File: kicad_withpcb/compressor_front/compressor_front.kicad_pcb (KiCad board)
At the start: 2 copper layers, 35 x 110 mm, 33 parts, among them J1 MAIN BOARD, SW1 BYPASS, SW2 INT/EXT, SW3 HPF DEFEAT, SW4 LINK, U10 LM3915, U9 LM3914

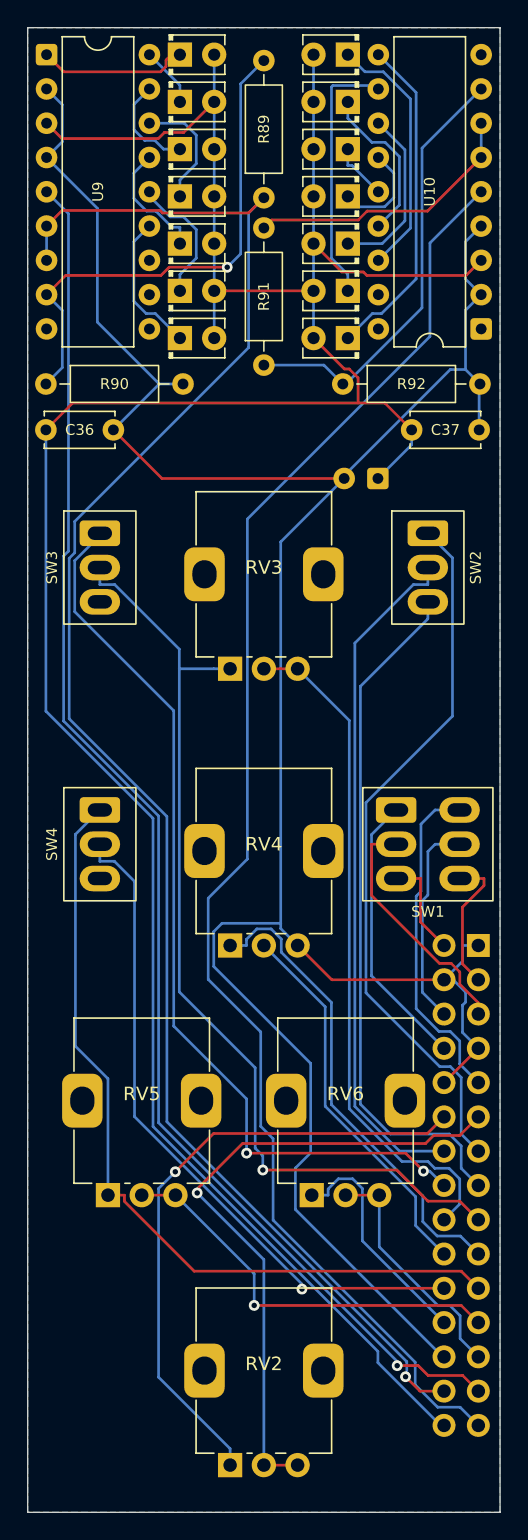
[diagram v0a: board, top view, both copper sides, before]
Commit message: Simulate the compressor, fix its values, and fit Altronics parts (#5)
* Make the schematic simulate in KiCad, and add the simulation results

Every part on the kicad/ sheets now has a SPICE model (Sim.* fields, models in
kicad/sim/compressor_models.lib), the connectors are excluded from simulation, and the
root sheet carries a test bench: the rack's supplies, a balanced source, a load and the
knob settings as .param lines. The netlist is unchanged.

tools/add_sim_models.py writes the fields. tools/sim/run_all.py exports the netlist with
kicad-cli and runs the characterisation in ngspice; kicad/sim/README.md has how to run
it in KiCad and what it found.

* Bring the compressor's values in line with the design targets

Through gain: R21/R22 3k3 to 6k8 halves the recovery amp's gain, so the
module is unity balanced in to out and BYPASS matches; R36 100k to 200k
keeps the detector's level. Bass: C9/C10 2u2 to 4u7 with the larger
input resistors puts the -3 dB point near 5 Hz.
Threshold: RV3 1M linear to 250k audio taper and R35 20k to 2k4 spread
about -20 to +20 dBu over the knob. R60 47k to 24k sets the resting
steer near 150 mV.
Timing: R45/R46/RV5 and R47/RV6/R74 scaled up to match the RC targets
with the same C15.

Same changes on the sheets, both boards and design.py. The simulation's
pot model gains an audio taper, and the burst test now runs at half
threshold.

* Carry the new values onto both boards' schematics and layouts

* Retune attack and release: R45 220R, R46 47R, RV5 10k, R47 15k

The first pass ran the attack too slow (9 to 103 ms against a 2.7 to
50 ms target). Results are regenerated in the next commit.

* Regenerate the simulation results for the new values

* Stop the fast-attack overshoot: C22 47u to 4u7

C22 made STA lag STB by about 60 ms, so when CTRL-B pulled the
reference node down the steering kept moving after the control
voltage had settled, overshooting by up to 20 dB. With 4u7 the two
sides track and the overshoot is about 1 dB. RV5 back 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
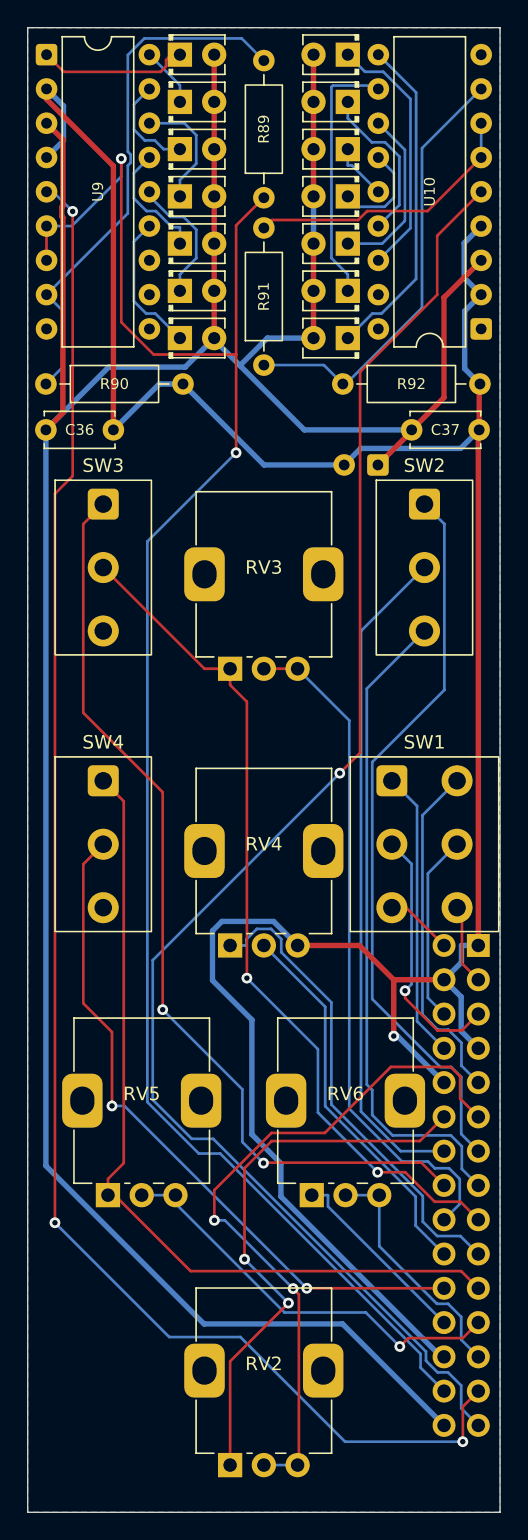
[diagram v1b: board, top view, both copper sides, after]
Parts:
- RV3: value 1M -> 100kA
- RV5: value 4k7 -> 10k
- RV6: value 220k -> 1M
- SW1: footprint compressor_front:SW_Toggle_SubMini_DPDT_Jaycar_ST0310 -> compressor_front:SW_Toggle_Mini_DPDT_Salecom_S1350
- SW2, SW3, SW4: footprint compressor_front:SW_Toggle_SubMini_SPDT_Jaycar_ST0300 -> compressor_front:SW_Toggle_Mini_SPDT_Salecom_S1315
- moved C38 1.00 mm to (127.5, 84.4)
- moved SW1 0.25 mm to (130.9, 112.5)
- moved SW2 0.25 mm to (130.9, 92.0)
- moved SW3 0.25 mm to (107.2, 92.0)
- moved SW4 0.25 mm to (107.2, 112.5)
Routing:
- net GR_METER: track 104.8 -> 119.2 mm, vias 1 -> 3
- net +16V: track 203.1 -> 215.2 mm
- net AGND: track 189.2 -> 198.7 mm, vias 0 -> 1
- net HPF_B: track 71.5 -> 63.3 mm, vias 1 -> 2
- net GR_REF: track 126.7 -> 134.6 mm, vias 1 -> 2
- net MAKEUP_FB: track 46.0 -> 41.5 mm, vias 1 -> 2
- net IN-: track 10.5 -> 5.99 mm
- net LVL_METER: track 109.0 -> 112.9 mm, vias 0 -> 1
- net OUT-A: track 48.0 -> 51.8 mm, vias 1 -> 2
- net TIMING: track 17.3 -> 14.2 mm
- net KEY: track 51.5 -> 48.8 mm
- net IN+: track 7.49 -> 5.02 mm
- net OUT-: track 15.4 -> 14.0 mm
- net HPF_A: track 67.6 -> 69.1 mm
- net LINK_SW: track 60.9 -> 62.3 mm
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
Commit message: Two LM3914 meters with ten LEDs each, simulated (#6)
* Swap the level meter's LM3915 for an LM3914 on outputs 1-7

Nobody stocks the LM3915, so U10 becomes a second LM3914. The LEDs move
to outputs 1-7 and outputs 8-10 join the top LED, giving a 17 dB scale
with no added parts. Front board LVL tracks re-routed; BOM regenerated.

* Give both meters ten LEDs and simulate them

Adds D27-D29 (GR outputs 8-10) and D37-D39 (LVL outputs 8-10) on all three
schematics. The front board's meter columns move to a 3.0 mm pitch with
LVL output 10 at the top; R90/R92 move to a 7.62 mm footprint and C38
turns to clear the LEDs; the affected nets were re-routed. R92 becomes 4k7
so RV8 can set the top LED at +18 dBu. The panel gets the six extra holes.
The LM3914 sim model now has its comparators and LED current sinks, and
tools/sim/meters.py simulates both meters.

* Write up the meter simulation
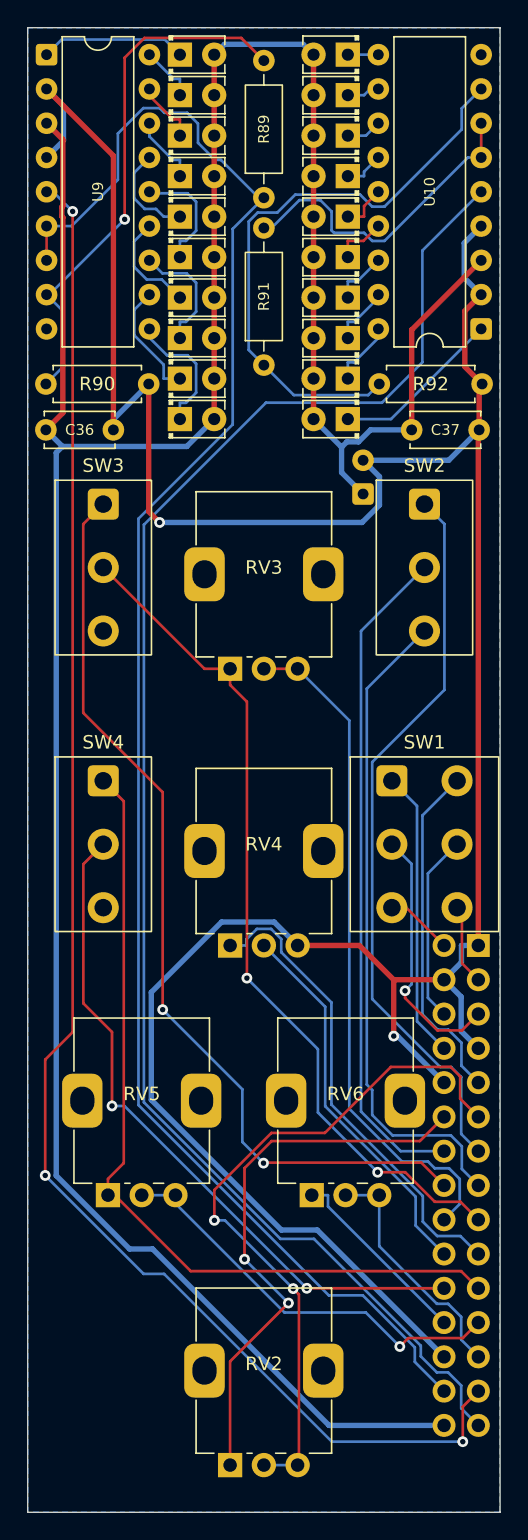
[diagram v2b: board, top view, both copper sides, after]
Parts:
- added D27: meter, LED_THT:LED_D2.0mm_W4.0mm_H2.8mm_FlatTop, F.Cu at (112.8, 75.0)
- added D28: meter, LED_THT:LED_D2.0mm_W4.0mm_H2.8mm_FlatTop, F.Cu at (112.8, 78.0)
- added D29: meter, LED_THT:LED_D2.0mm_W4.0mm_H2.8mm_FlatTop, F.Cu at (112.8, 81.0)
- added D37: meter, LED_THT:LED_D2.0mm_W4.0mm_H2.8mm_FlatTop, F.Cu at (125.3, 60.0)
- added D38: meter, LED_THT:LED_D2.0mm_W4.0mm_H2.8mm_FlatTop, F.Cu at (125.3, 57.0)
- added D39: meter, LED_THT:LED_D2.0mm_W4.0mm_H2.8mm_FlatTop, F.Cu at (125.3, 54.0)
- R90: footprint Resistor_THT:R_Axial_DIN0207_L6.3mm_D2.5mm_P10.16mm_Horizontal -> Resistor_THT:R_Axial_DIN0207_L6.3mm_D2.5mm_P7.62mm_Horizontal
- R92: value 8k2 -> 4k7; footprint Resistor_THT:R_Axial_DIN0207_L6.3mm_D2.5mm_P10.16mm_Horizontal -> Resistor_THT:R_Axial_DIN0207_L6.3mm_D2.5mm_P7.62mm_Horizontal
- U10: value LM3915 -> LM3914
- moved D30 27.0 mm to (125.3, 81.0)
- moved D31 20.5 mm to (125.3, 78.0)
- moved D32 14.0 mm to (125.3, 75.0)
- moved D36 12.0 mm to (125.3, 63.0)
- moved D33 7.50 mm to (125.3, 72.0)
- moved D35 5.50 mm to (125.3, 66.0)
- moved D26 3.00 mm to (112.8, 72.0)
- moved R92 2.70 mm to (127.6, 78.4)
- moved D25 2.50 mm to (112.8, 69.0)
- moved C38 2.42 mm to (126.4, 86.5), turned to 90 degrees
- moved D24 2.00 mm to (112.8, 66.0)
- moved D23 1.50 mm to (112.8, 63.0)
- moved D22 1.00 mm to (112.8, 60.0)
- moved D34 1.00 mm to (125.3, 69.0)
- moved D21 0.50 mm to (112.8, 57.0)
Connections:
- U10 pad 1: unconnected-(U10-LED1-Pad1) -> LVL1
- U10 pad 10: LVL7 -> LVL10
- U10 pad 11: LVL6 -> LVL9
- U10 pad 12: LVL5 -> LVL8
- U10 pad 13: LVL4 -> LVL7
- U10 pad 14: LVL3 -> LVL6
- U10 pad 15: LVL2 -> LVL5
- U10 pad 16: LVL1 -> LVL4
- U10 pad 17: unconnected-(U10-LED3-Pad17) -> LVL3
- U10 pad 18: unconnected-(U10-LED2-Pad18) -> LVL2
- U9 pad 10: unconnected-(U9-LED10-Pad10) -> GR10
- U9 pad 11: unconnected-(U9-LED9-Pad11) -> GR9
- U9 pad 12: unconnected-(U9-LED8-Pad12) -> GR8
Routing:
- net LVL7: track 24.7 -> 3.02 mm
- net AGND: track 198.7 -> 217.1 mm, vias 1 -> 2
- net LVL6: track 19.2 -> 3.48 mm
- net LVL_REFADJ: track 32.7 -> 43.9 mm
- net GR10: track 0.00 -> 9.77 mm
- net LVL5: track 13.0 -> 3.92 mm
- net GR8: track 0.00 -> 9.01 mm
- net GR9: track 0.00 -> 8.79 mm
- net LVL2: track 12.0 -> 4.88 mm
- net LVL1: track 18.9 -> 12.6 mm
- net LVL_METER: track 112.9 -> 119.0 mm, vias 1 -> 0
- net GR4: track 8.88 -> 5.16 mm
- net GR_REF: track 134.6 -> 130.9 mm, vias 2 -> 0
- net LVL4: track 7.46 -> 4.11 mm
- net LVL_REF: track 20.8 -> 24.1 mm
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
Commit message: Re-route the main board, reverse RATIO, and re-plot the Gerbers for both boards (#7)
* Re-plot the Gerbers for both boards from the current layout

The committed main-board Gerbers were plotted on 2026-10-01, before the film-cap
re-place and re-route, so 119 of their holes no longer match the board. Re-plot
them from the current board, add the front board's set, and zip each for the fab.

tools/plot_fab.sh does both boards in one go so the zips can be refreshed after
every board change. The README gets an Ordering section with the fab settings.

* Re-route the main board: paired IN/OUT, one-piece ground pour

IN+/IN- and OUT+/OUT- run as pairs 0.6 mm apart on the top layer, with
one via each on IN- and OUT- beside the edge fingers. Most other tracks
moved to the top so the bottom AGND pour is one piece (was seven).
DRC 0 errors, 0 unconnected, 0 schematic parity issues. Gerbers re-plotted.

* Swap RATIO's outer pins so clockwise gives a harder ratio

RV4 pin 1 is now AGND and pin 3 RATIO_CW on all three schematics and the
front board (symbol mirrored, front-board tracks re-routed at RV4).
The sim model reads POS={1-RATIO}, so RATIO keeps its meaning and the
results are unchanged. Front-board DRC 0 errors, 0 unconnected, 0 parity;
front Gerbers re-plotted.
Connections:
- RV4 pad 1: RATIO_CW -> AGND
- RV4 pad 3: AGND -> RATIO_CW
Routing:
- net RATIO_CW: track 35.3 -> 29.4 mm
- net AGND: track 217.1 -> 220.6 mm
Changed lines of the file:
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@@
 			(layers "*.Cu" "*.Mask")
 			(remove_unused_layers no)
-			(net "RATIO_CW")
+			(net "AGND")
 		)
 		(pad "2" thru_hole circle
@@
 			(layers "*.Cu" "*.Mask")
 			(remove_unused_layers no)
-			(net "AGND")
+			(net "RATIO_CW")
 		)
 		(pad "MP" thru_hole roundrect
@@
 	)
 	(gr_circle
-		(center 114.1 54) (end 115.2 54)
+		(center 114.1 54)
+		(end 115.2 54)
 		(stroke
 			(width 0.1)
@@
 	)
 	(gr_circle
-		(center 114.1 57) (end 115.2 57)
+		(center 114.1 57)
+		(end 115.2 57)
 		(stroke
 			(width 0.1)
@@
 	)
 	(gr_circle
-		(center 114.1 60) (end 115.2 60)
+		(center 114.1 60)
+		(end 115.2 60)
 		(stroke
 			(width 0.1)
@@
 	)
 	(gr_circle
-		(center 114.1 63) (end 115.2 63)
+		(center 114.1 63)
+		(end 115.2 63)
 		(stroke
 			(width 0.1)
@@
 	)
 	(gr_circle
-		(center 114.1 66) (end 115.2 66)
+		(center 114.1 66)
+		(end 115.2 66)
 		(stroke
 			(width 0.1)
@@
 	)
 	(gr_circle
-		(center 114.1 69) (end 115.2 69)
+		(center 114.1 69)
+		(end 115.2 69)
 		(stroke
 			(width 0.1)
@@
 	)
 	(gr_circle
-		(center 114.1 72) (end 115.2 72)
+		(center 114.1 72)
+		(end 115.2 72)
 		(stroke
 			(width 0.1)
@@
 	)
 	(gr_circle
-		(center 114.1 75) (end 115.2 75)
+		(center 114.1 75)
+		(end 115.2 75)
 		(stroke
 			(width 0.1)
@@
 	)
 	(gr_circle
-		(center 114.1 78) (end 115.2 78)
+		(center 114.1 78)
+		(end 115.2 78)
 		(stroke
 			(width 0.1)
@@
 	)
 	(gr_circle
-		(center 114.1 81) (end 115.2 81)
+		(center 114.1 81)
+		(end 115.2 81)
 		(stroke
 			(width 0.1)
@@
 	)
 	(gr_circle
-		(center 124 54) (end 125.1 54)
+		(center 119.05 43.96)
+		(end 120.64 43.96)
 		(stroke
 			(width 0.1)
@@
 	)
 	(gr_circle
-		(center 124 57) (end 125.1 57)
+		(center 119.05 43.96)
+		(end 121.91 43.96)
 		(stroke
 			(width 0.1)
@@
 	)
 	(gr_circle
-		(center 124 60) (end 125.1 60)
+		(center 119.05 92)
+		(end 122.65 92)
 		(stroke
 			(width 0.1)
@@
 	)
 	(gr_circle
-		(center 124 63) (end 125.1 63)
+		(center 119.05 112.5)
+		(end 122.65 112.5)
 		(stroke
 			(width 0.1)
@@
 	)
 	(gr_circle
-		(center 124 66) (end 125.1 66)
+		(center 119.05 151)
+		(end 122.65 151)
 		(stroke
 			(width 0.1)
@@
 	)
 	(gr_circle
-		(center 124 69) (end 125.1 69)
+		(center 119.05 169.39)
+		(end 120.64 169.39)
 		(stroke
 			(width 0.1)
@@
 	)
 	(gr_circle
-		(center 124 72) (end 125.1 72)
+		(center 119.05 169.39)
+		(end 121.91 169.39)
 		(stroke
 			(width 0.1)
@@
 	)
 	(gr_circle
-		(center 124 75) (end 125.1 75)
+		(center 124 54)
+		(end 125.1 54)
 		(stroke
 			(width 0.1)
@@
 	)
 	(gr_circle
-		(center 124 78) (end 125.1 78)
+		(center 124 57)
+		(end 125.1 57)
 		(stroke
 			(width 0.1)
@@
 	)
 	(gr_circle
-		(center 124 81) (end 125.1 81)
+		(center 124 60)
+		(end 125.1 60)
 		(stroke
 			(width 0.1)
@@
 	)
 	(gr_circle
-		(center 119.05 43.96)
-		(end 120.64 43.96)
+		(center 124 63)
+		(end 125.1 63)
 		(stroke
 			(width 0.1)
@@
 	)
 	(gr_circle
-		(center 119.05 43.96)
-		(end 121.91 43.96)
+		(center 124 66)
+		(end 125.1 66)
 		(stroke
 			(width 0.1)
@@
 	)
 	(gr_circle
-		(center 119.05 92)
-		(end 122.65 92)
+		(center 124 69)
+		(end 125.1 69)
 		(stroke
 			(width 0.1)
@@
 	)
 	(gr_circle
-		(center 119.05 112.5)
-		(end 122.65 112.5)
+		(center 124 72)
+		(end 125.1 72)
 		(stroke
 			(width 0.1)
@@
 	)
 	(gr_circle
-		(center 119.05 151)
-		(end 122.65 151)
+		(center 124 75)
+		(end 125.1 75)
 		(stroke
 			(width 0.1)
@@
 	)
 	(gr_circle
-		(center 119.05 169.39)
-		(end 120.64 169.39)
+		(center 124 78)
+		(end 125.1 78)
 		(stroke
 			(width 0.1)
@@
 	)
 	(gr_circle
-		(center 119.05 169.39)
-		(end 121.91 169.39)
+		(center 124 81)
+		(end 125.1 81)
 		(stroke
 			(width 0.1)
@@
 	)
 	(segment
-		(start 121.55 120)
-		(end 126.1318 120)
-		(width 0.4)
-		(layer "F.Cu")
-		(net "AGND")
-	)
-	(segment
 		(start 135.22 78.4)
 		(end 135 78.62)
@@
 	)
 	(segment
-		(start 126.1318 120)
-		(end 128.6718 122.54)
+		(start 135 78.62)
+		(end 135 81.8)
 		(width 0.4)
 		(layer "F.Cu")
@@
 	)
 	(segment
-		(start 135 78.62)
-		(end 135 81.8)
+		(start 128.6718 122.54)
+		(end 132.4 122.54)
 		(width 0.4)
 		(layer "F.Cu")
@@
 	)
 	(segment
-		(start 128.6718 122.54)
-		(end 132.4 122.54)
+		(start 116.55 120)
+		(end 116.55 123.6)
 		(width 0.4)
 		(layer "F.Cu")
@@
 	)
 	(segment
+		(start 116.55 123.6)
+		(end 127.6118 123.6)
+		(width 0.4)
+		(layer "F.Cu")
+		(net "AGND")
+	)
+	(segment
+		(start 127.6118 123.6)
+		(end 128.671799 122.54)
+		(width 0.4)
+		(layer "F.Cu")
+		(net "AGND")
+	)
+	(segment
 		(start 110.52 87.8563)
 		(end 111.3236 88.6599)
@@
 	)
 	(segment
+		(start 116.55 120)
+		(end 116.55 120)
+		(width 0.4)
+		(layer "B.Cu")
+		(net "AGND")
+	)
+	(segment
 		(start 135.15 66.7)
 		(end 133.8939 67.9561)
@@
 	)
 	(segment
+		(start 116.55 120)
+		(end 115.9162 118.265)
+		(width 0.4)
+		(layer "B.Cu")
+		(net "AGND")
+	)
+	(segment
 		(start 133.8939 67.9561)
 		(end 133.8939 70.5239)
@@
 	)
 	(segment
-		(start 119.815 118.265)
-		(end 121.55 120)
-		(width 0.4)
-		(layer "B.Cu")
-		(net "AGND")
-	)
-	(segment
 		(start 110.7097 131.4428)
 		(end 110.7097 123.4715)
@@
 	)
 	(segment
-		(start 115.9162 118.265)
-		(end 119.815 118.265)
-		(width 0.4)
-		(layer "B.Cu")
-		(net "AGND")
-	)
-	(segment
 		(start 132.4 122.54)
 		(end 133.6883 121.2517)
@@
 	)
 	(segment
-		(start 118.535 118.772)
-		(end 119.584 118.772)
-		(width 0.2)
-		(layer "B.Cu")
-		(net "RATIO_CW")
-	)
-	(segment
-		(start 117.762 120)
-		(end 117.762 119.546)
-		(width 0.2)
-		(layer "B.Cu")
-		(net "RATIO_CW")
-	)
-	(segment
 		(start 124.054 124.218)
 		(end 124.054 131.79)
@@
 	)
 	(segment
-		(start 117.762 119.546)
-		(end 118.535 118.772)
+		(start 121.55 121.714)
+		(end 124.054 124.218)
 		(width 0.2)
 		(layer "B.Cu")
@@
 	)
 	(segment
-		(start 120.338 119.526)
-		(end 120.338 120.502)
+		(start 121.55 120)
+		(end 121.55 121.714)
 		(width 0.2)
 		(layer "B.Cu")
@@
 	)
 	(segment
-		(start 119.584 118.772)
-		(end 120.338 119.526)
-		(width 0.2)
-		(layer "B.Cu")
-		(net "RATIO_CW")
-	)
-	(segment
-		(start 116.55 120)
-		(end 117.762 120)
-		(width 0.2)
-		(layer "B.Cu")
-		(net "RATIO_CW")
-	)
-	(segment
 		(start 130.827 138.563)
 		(end 130.827 140.468)
 		(width 0.2)
 		(layer "B.Cu")
-		(net "RATIO_CW")
-	)
-	(segment
-		(start 120.338 120.502)
-		(end 124.054 124.218)
-		(width 0.2)
-		(layer "B.Cu")
